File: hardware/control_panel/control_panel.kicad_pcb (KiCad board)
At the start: 2 copper layers, 65 x 58 mm, 155 parts, among them J1 display, J10 Conn_01x03, J11 Conn_02x04_Odd_Even, J12 AVR-ISP-6, J13 motion and brightness sensors, J14 Conn_01x07, J15 Screw_Terminal_01x07, J2 Conn_02x02_Odd_Even, J3 40HAT, J4 Screw_Terminal_CAN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

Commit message: hw layout
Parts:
- removed J11: Conn_02x04_Odd_Even, Connector_PinSocket_2.54mm:PinSocket_2x04_P2.54mm_Vertical
- removed J14: Conn_01x07, Connector_PinHeader_2.54mm:PinHeader_1x07_P2.54mm_Vertical
- removed J15: Screw_Terminal_01x07, TerminalBlock_Phoenix:TerminalBlock_Phoenix_MPT-0,5-7-2.54_1x07_P2.54mm_Horizontal
- added C2: 22u, Capacitor_SMD:C_0805_2012Metric, F.Cu at (80.3, 78.8)
- added C39: 1u, Capacitor_SMD:C_0603_1608Metric, F.Cu at (111.0, 76.3)
- added C6: 22u, Capacitor_SMD:C_0805_2012Metric, F.Cu at (80.3, 80.8)
- added U9: NRF24L01_Breakout, project_footprints:nRF24L01_Breakout, F.Cu at (127.5, 75.8)
- C13: value 22u -> 1u; footprint Capacitor_SMD:C_0805_2012Metric -> Capacitor_SMD:C_0603_1608Metric
- C17, C3: footprint Capacitor_THT:CP_Radial_D10.0mm_P5.00mm -> Capacitor_THT:CP_Radial_D8.0mm_P3.50mm
- D2: footprint Package_TO_SOT_SMD:SOT-23 -> Package_TO_SOT_SMD:SOT-23_Handsoldering
- D5, D6, D7: value SM712_SOT23 -> D; footprint Package_TO_SOT_SMD:SOT-23 -> Package_TO_SOT_SMD:SOT-23_Handsoldering
- F1: moved to F.Cu
- J12: footprint project_footprints:Tag-Connect_TC2030-IDC-NL_2x03_P1.27mm_Vertical -> Connector_PinHeader_2.54mm:PinHeader_2x03_P2.54mm_Vertical
- J3: footprint Connector_PinSocket_2.54mm:PinSocket_2x20_P2.54mm_Vertical -> project_footprints:raspberry_pi
- L2: footprint Inductor_THT:L_Radial_D7.5mm_P5.00mm_Fastron_07P -> Inductor_THT:L_Radial_D7.5mm_P3.50mm_Fastron_07P
- U2: footprint Package_TO_SOT_SMD:SOT-563 -> Package_TO_SOT_SMD:SOT-363_SC-70-6
- moved JP2 114.0 mm to (103.0, 97.6), turned to 180 degrees
- moved JP3 113.5 mm to (103.0, 100.6), turned to 180 degrees
- moved JP6 113.1 mm to (103.0, 103.6), turned to 180 degrees
- moved U8 88.5 mm to (104.0, 115.1)
- moved C1 79.3 mm to (121.8, 115.6), turned to 180 degrees
- moved L10 73.0 mm to (121.8, 112.1), turned to 90 degrees
- moved Q1 64.2 mm to (134.5, 77.3), turned to 180 degrees
- moved R41 64.0 mm to (106.4, 67.8), turned to 180 degrees
- moved R30 60.9 mm to (133.5, 74.1), turned to -90 degrees
- moved R27 58.6 mm to (133.5, 72.2), turned to -90 degrees
- moved R29 57.9 mm to (135.5, 74.1), turned to -90 degrees
- moved R28 55.4 mm to (135.5, 72.2), turned to -90 degrees
- moved JP5 54.7 mm to (133.5, 68.8), turned to -90 degrees
- moved JP4 51.3 mm to (135.5, 68.8), turned to -90 degrees
- moved C13 32.2 mm to (104.0, 92.3)
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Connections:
- C13 pad 1: +5V -> GND
- C13 pad 2: GND -> +5V
- C58 pad 1: VBUS -> /CAN/Vin
- D1 pad 1: VBUS -> /CAN/Vin
- J13 pad 2: /SCL -> /MOT
- J13 pad 3: /SDA -> /SCL
- J13 pad 4: /MOT -> /SDA
- J3 pad 7: unconnected-(J3-BCM4-Pad7) -> /MOT
- R2 pad 2: /I2C/SDA_{X} -> /I2C/SDA_{T}
- R3 pad 2: /I2C/SCL_{X} -> /I2C/SCL_{T}
- R39 pad 2: /I2C/INT_{X} -> /I2C/INT
- U3 pad 13: /UC.IRQ -> /UC.CE
- U3 pad 14: /UC.CE -> /UC.IRQ
- U3 pad 7: /RF.CE -> /RF.IRQ
- U3 pad 8: /RF.IRQ -> /RF.CE
- U6 pad 1: /UC.IRQ -> /UC_INT
- U6 pad 3: unconnected-(U6-PE0-Pad3) -> /UC.IRQ
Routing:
- net +5V: track 55.3 -> 190.3 mm, vias 0 -> 8
- net /CLK: track 13.4 -> 87.3 mm
- net /SDA: track 25.7 -> 80.7 mm, vias 0 -> 6
- net /PI_INT: track 0.00 -> 51.2 mm, vias 0 -> 4
- net /SCL: track 21.9 -> 67.7 mm, vias 0 -> 6
- net /ADC: track 15.7 -> 57.2 mm
- net +3.3V: track 1.86 -> 41.0 mm
- net /DAC: track 14.8 -> 51.4 mm
- net /LRC: track 16.0 -> 44.5 mm
- net /PI_TX: track 0.00 -> 28.0 mm
- net /UC.IRQ: track 0.00 -> 27.4 mm
- net /CAN/Vin: track 3.95 -> 30.0 mm
- net /PI_RX: track 0.00 -> 25.7 mm
- net /~{INT}: track 0.00 -> 25.4 mm
- net /UC_INT: track 0.00 -> 23.0 mm, vias 0 -> 2
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- added copper zone on F.Cu, net +24V
- removed copper zone on B.Cu, net +5V
- removed copper zone on B.Cu, net /Vreg/SW
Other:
- board text added: "RUN PEN"
- board text added: "uC|Pi I2C"

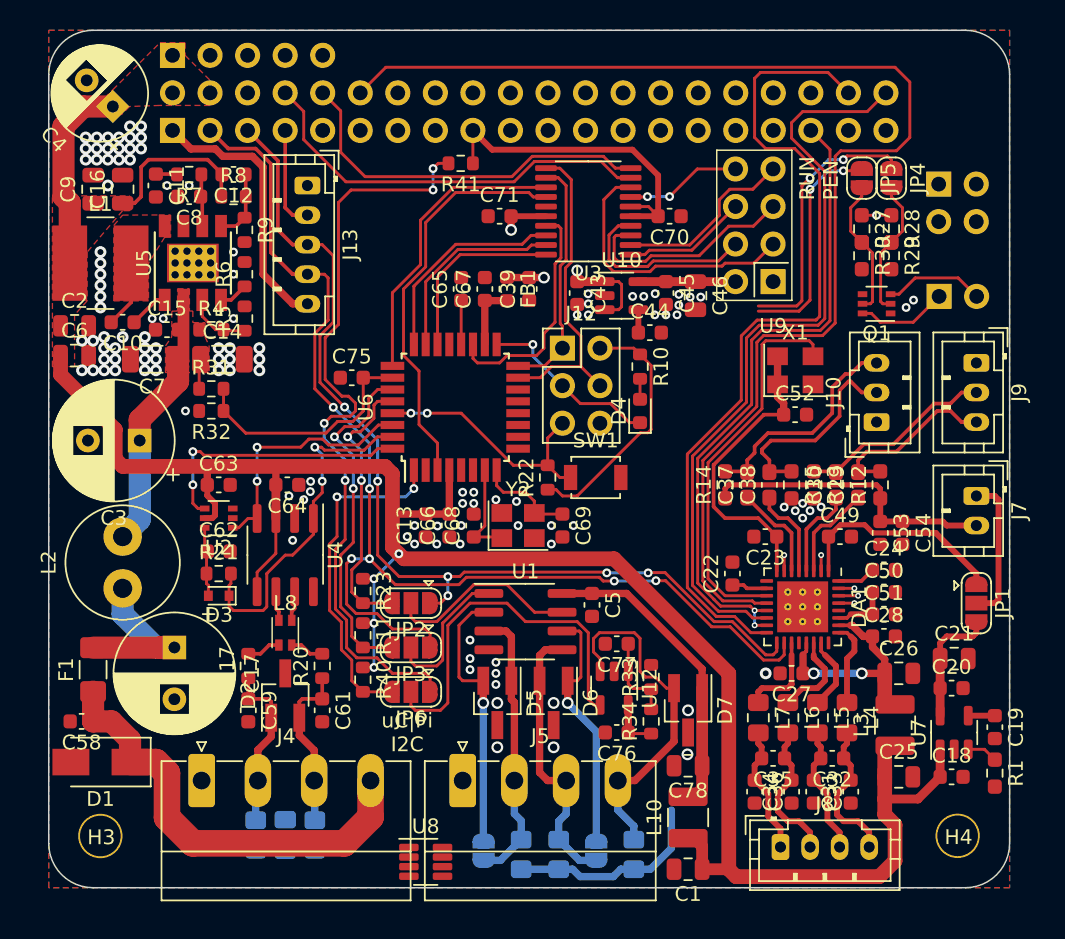
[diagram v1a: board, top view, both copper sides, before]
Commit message: led balance and corridor ready
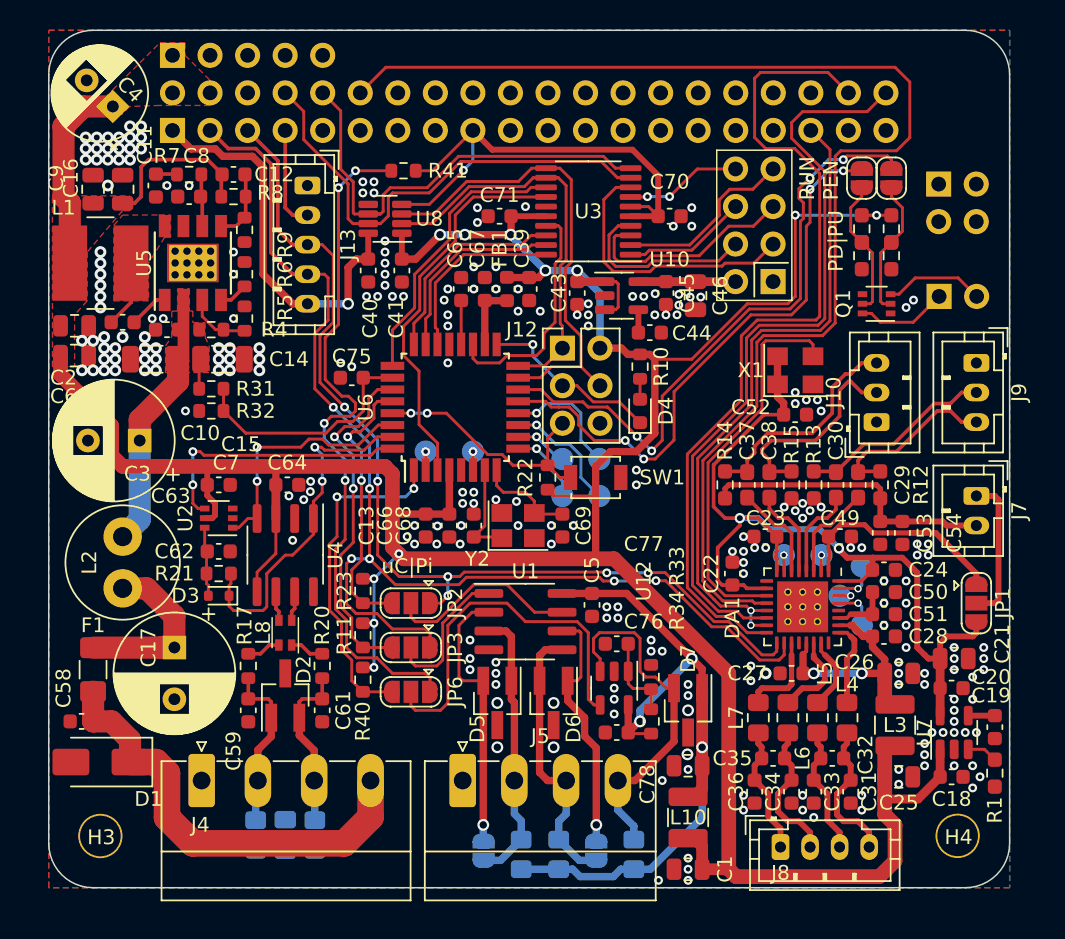
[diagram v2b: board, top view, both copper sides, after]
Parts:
- added C40: 100n, Capacitor_SMD:C_0603_1608Metric, F.Cu at (100.2, 75.1)
- added C41: 100n, Capacitor_SMD:C_0603_1608Metric, F.Cu at (102.4, 75.1)
- added TP1: PB0, project_footprints:TestPoint_Pad_D1.5mm, B.Cu at (115.8, 87.8)
- added TP10: LIN3, project_footprints:TestPoint_Pad_D1.5mm, B.Cu at (130.8, 94.3)
- added TP11: RIN3, project_footprints:TestPoint_Pad_D1.5mm, B.Cu at (128.3, 94.3)
- added TP2: PD4, project_footprints:TestPoint_Pad_D1.5mm, B.Cu at (104.0, 87.3)
- added TP3: PD5, project_footprints:TestPoint_Pad_D1.5mm, B.Cu at (113.3, 90.3)
- added TP4: PD6, project_footprints:TestPoint_Pad_D1.5mm, B.Cu at (113.3, 87.8)
- added TP5: PD7, project_footprints:TestPoint_Pad_D1.5mm, B.Cu at (115.8, 90.3)
- added TP6: PE1, project_footprints:TestPoint_Pad_D1.5mm, B.Cu at (107.2, 87.3)
- added TP7: HP_R, project_footprints:TestPoint_Pad_D1.5mm, B.Cu at (133.5, 99.1)
- added TP8: OUT3, project_footprints:TestPoint_Pad_D1.5mm, B.Cu at (132.0, 97.1)
- added TP9: HP_L, project_footprints:TestPoint_Pad_D1.5mm, B.Cu at (133.5, 95.1)
- DA1: footprint Package_DFN_QFN:QFN-32-1EP_5x5mm_P0.5mm_EP3.45x3.45mm_ThermalVias -> project_footprints:QFN-32-1EP_5x5mm_P0.5mm_EP3.45x3.45mm_ThermalVias
- Q1: value Q_Dual_NMOS_S1G1D2S2G2D1 -> 2N7002DW
- moved U8 43.6 mm to (101.3, 71.6), turned to 180 degrees
- moved R41 3.90 mm to (102.5, 68.3)
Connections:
- U6 pad 10: unconnected-(U6-PD6-Pad10) -> Net-(U6-PD6)
- U6 pad 11: /MCU/BT_1 -> Net-(U6-PD7)
- U6 pad 12: unconnected-(U6-PB0-Pad12) -> Net-(U6-PB0)
- U6 pad 13: unconnected-(U6-PB1-Pad13) -> /MCU/RUN
- U6 pad 14: unconnected-(U6-PB2-Pad14) -> /MCU/PEN
- U6 pad 2: /MCU/BT_0 -> Net-(U6-PD4)
- U6 pad 6: unconnected-(U6-PE1-Pad6) -> Net-(U6-PE1)
- U6 pad 9: unconnected-(U6-PD5-Pad9) -> Net-(U6-PD5)
- U8 pad 1: unconnected-(U8-VCCB-Pad1) -> +5V
- U8 pad 2: unconnected-(U8-B1-Pad2) -> /GW_RX
- U8 pad 3: unconnected-(U8-B2-Pad3) -> /GW_TX
- U8 pad 4: unconnected-(U8-OE-Pad4) -> +3.3V
- U8 pad 5: unconnected-(U8-GND-Pad5) -> GND
- U8 pad 6: unconnected-(U8-A2-Pad6) -> /PI_RX
- U8 pad 7: unconnected-(U8-A1-Pad7) -> /PI_TX
- U8 pad 8: unconnected-(U8-VCCA-Pad8) -> +3.3V
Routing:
- net +5V: track 190.3 -> 240.5 mm, vias 8 -> 11
- net +3.3VA: track 33.9 -> 61.2 mm, vias 0 -> 2
- net /MCU/RUN: track 15.5 -> 39.6 mm, vias 2 -> 4
- net /MCU/PEN: track 18.5 -> 42.3 mm, vias 2 -> 4
- net +3.3V: track 41.0 -> 60.4 mm, vias 0 -> 2
- net +5VD: track 38.1 -> 50.0 mm, vias 0 -> 3
- net /GW_RX: track 16.3 -> 27.3 mm
- net /GW_TX: track 21.7 -> 32.7 mm
- net Net-(U6-PB0): track 0.00 -> 8.41 mm, vias 0 -> 1
- net Net-(U6-PD7): track 0.00 -> 8.35 mm, vias 0 -> 1
- net /PI_RX: track 25.7 -> 31.1 mm
- net /PI_TX: track 28.0 -> 33.2 mm
- net Net-(U6-PD5): track 0.00 -> 5.17 mm, vias 0 -> 1
- net /PI_INT: track 51.2 -> 46.9 mm
- net Net-(U6-PD6): track 0.00 -> 3.62 mm, vias 0 -> 1
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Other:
- board text added: "PD|PU"
- board text added: "uC|Pi"
- board text removed: "uC|Pi I2C"
